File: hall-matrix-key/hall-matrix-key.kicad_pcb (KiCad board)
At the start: 2 copper layers, 178 x 59.9 mm, 18 parts, among them J1 Conn_01x06_Pin, J2 Conn_01x06_Pin, J3 Conn_01x06_Pin, J4 Conn_01x06_Pin, J5 Conn_01x01_Pin, J6 Conn_01x08_Pin

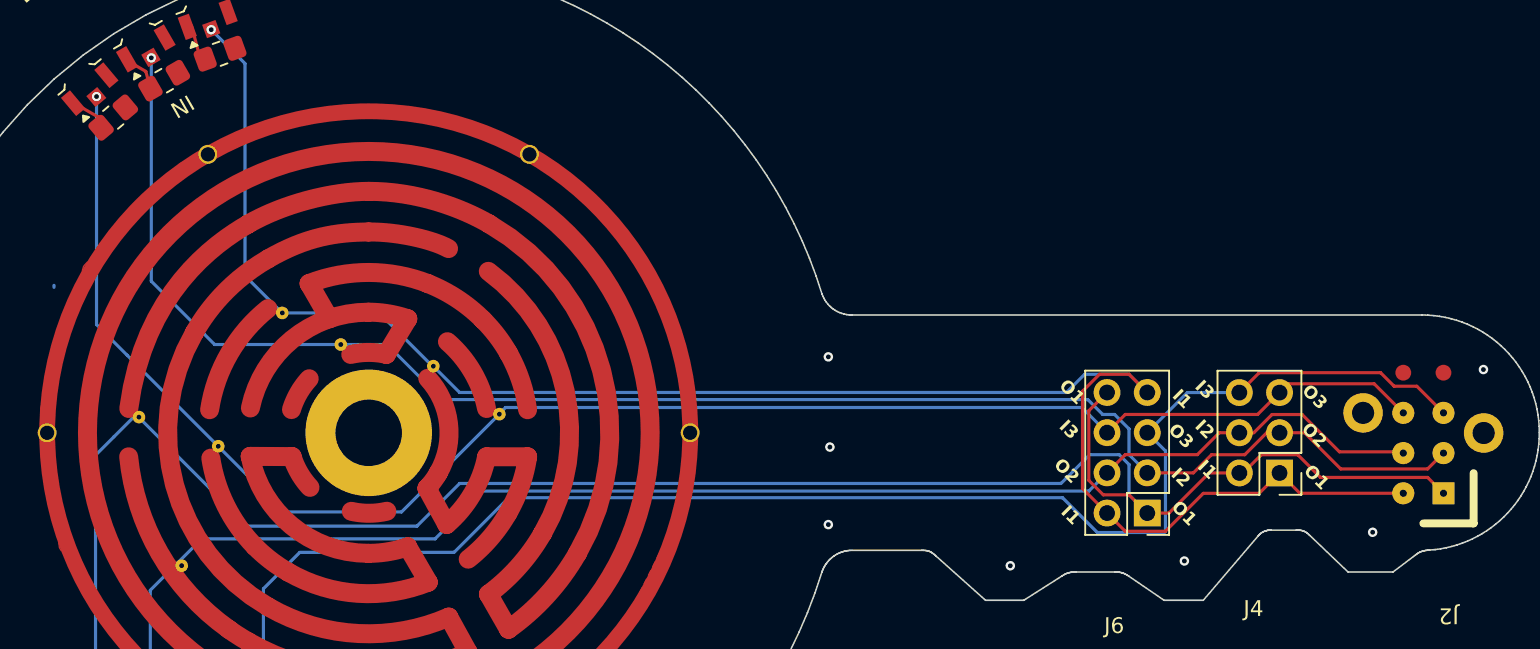
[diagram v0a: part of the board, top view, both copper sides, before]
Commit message: update for second, corrected batch.
series manufactured for WHY2025 have one pogo hole too small on the
rotator
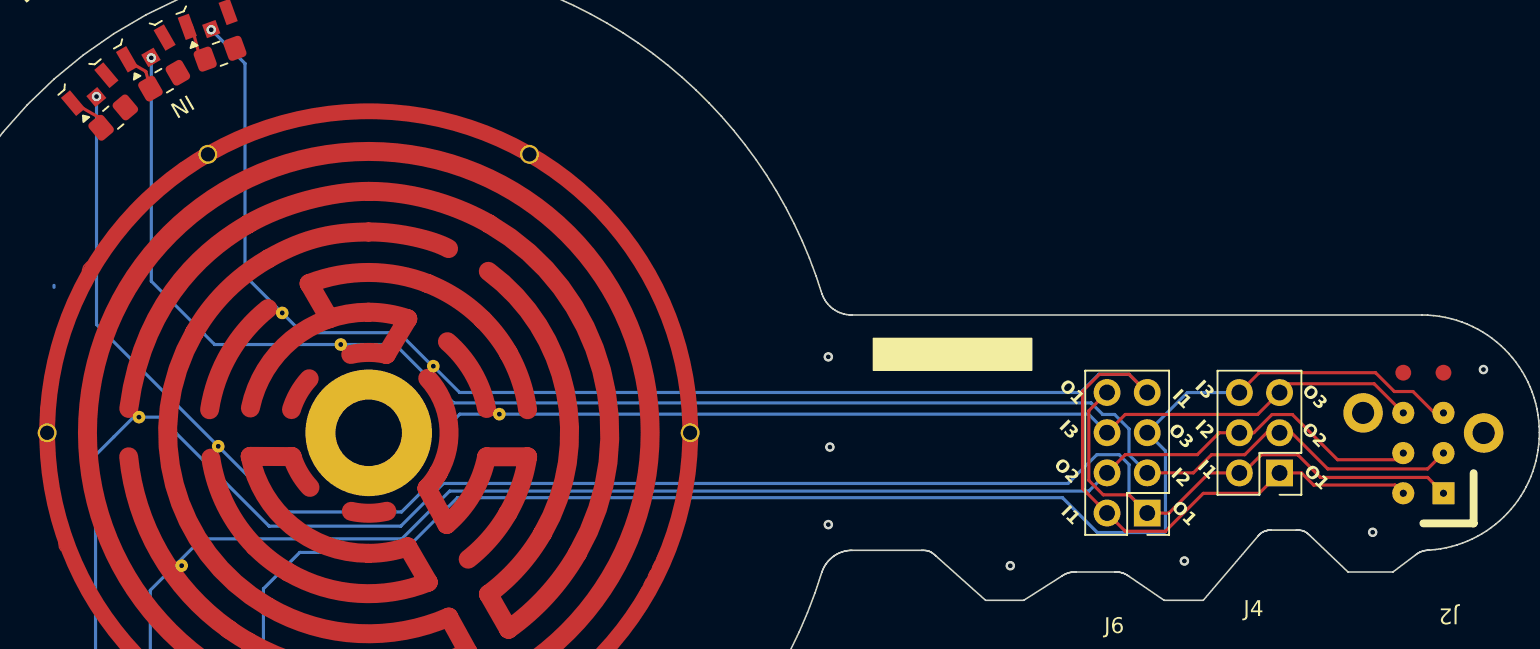
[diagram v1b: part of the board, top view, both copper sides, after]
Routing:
- net /I3: track 107.3 -> 108.5 mm
